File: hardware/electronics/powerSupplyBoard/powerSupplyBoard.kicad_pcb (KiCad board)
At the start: 4 copper layers, 100 x 50 mm, 119 parts, among them J1 USB_C_Receptacle_USB2.0, J10 1729018, J11 PREC002SAAN-RC, J3 615004143821, J4 PRPC009SBAN-M71RC, J5 Barrel_Jack_Switch, J6 S2B-PH-SM4-TB, J7 PREC002SAAN-RC, J8 PREC003SAAN-RC, J9 S3B-XH-SM4-TB, Q1 BUK961R6, Q2 CSD18532Q5B, Q3 CSD18532Q5B, Q4 BSS84, Q5 2N7002, Q6 2N7002, SW1 PTS647, SW2 SS-12D07, U1 STM32L052K6, U2 AP2112K-3.3, U3 SN65HVD230QDR, U4 BQ25798, U5 BQ76905, U6 BQ34Z100-R2, Y1 ECS-327ATQMV

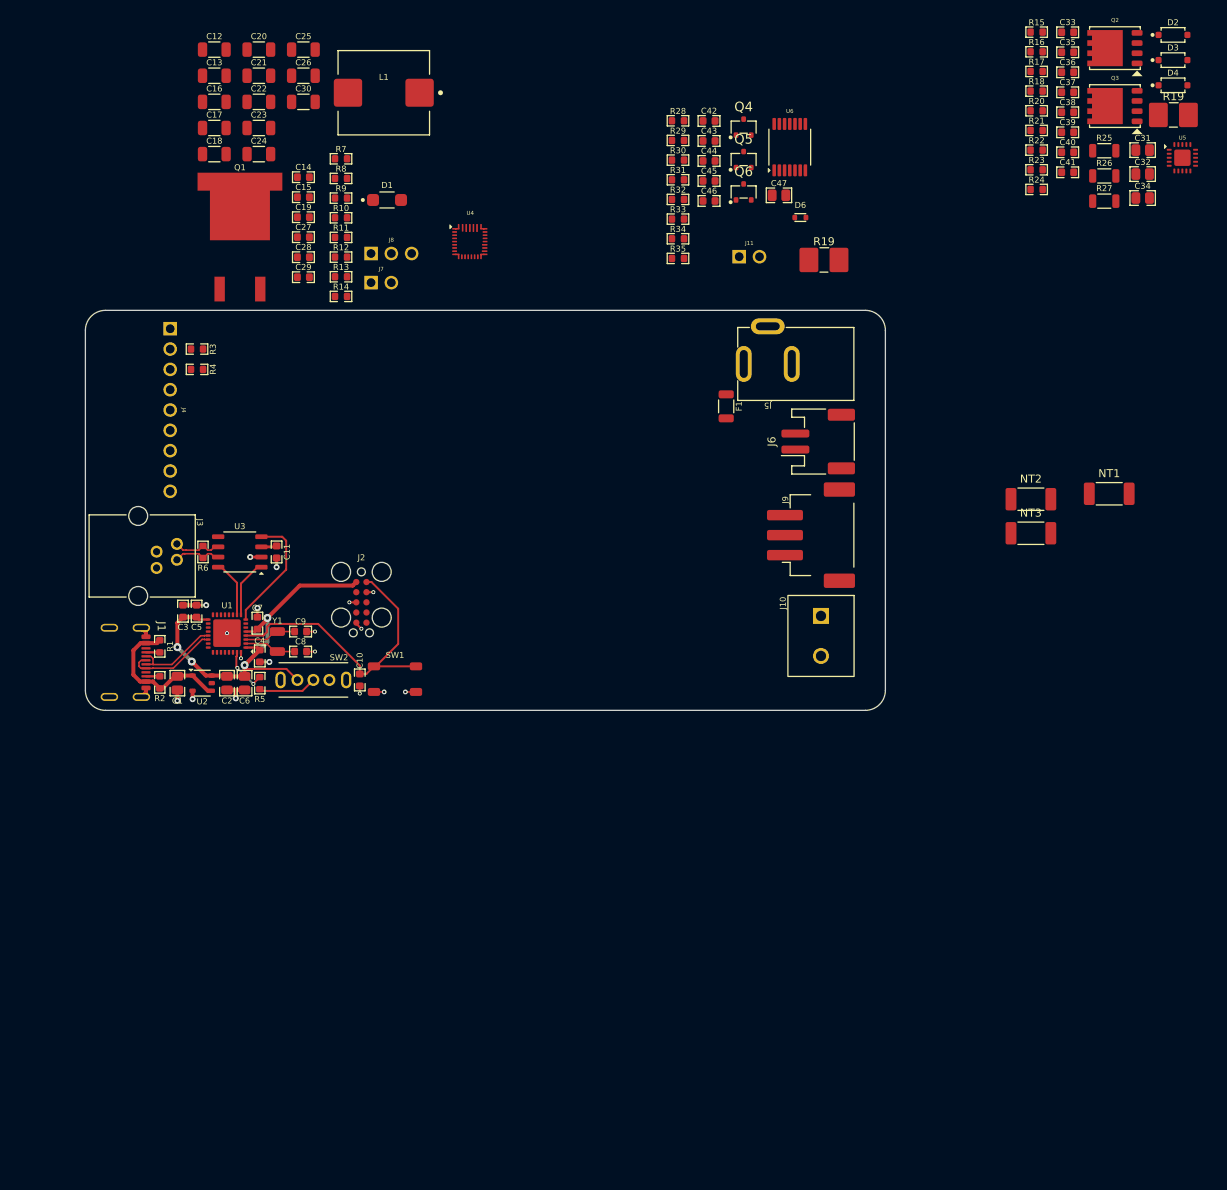
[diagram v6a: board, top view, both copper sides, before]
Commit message: re-synced board. adjusted reference labels
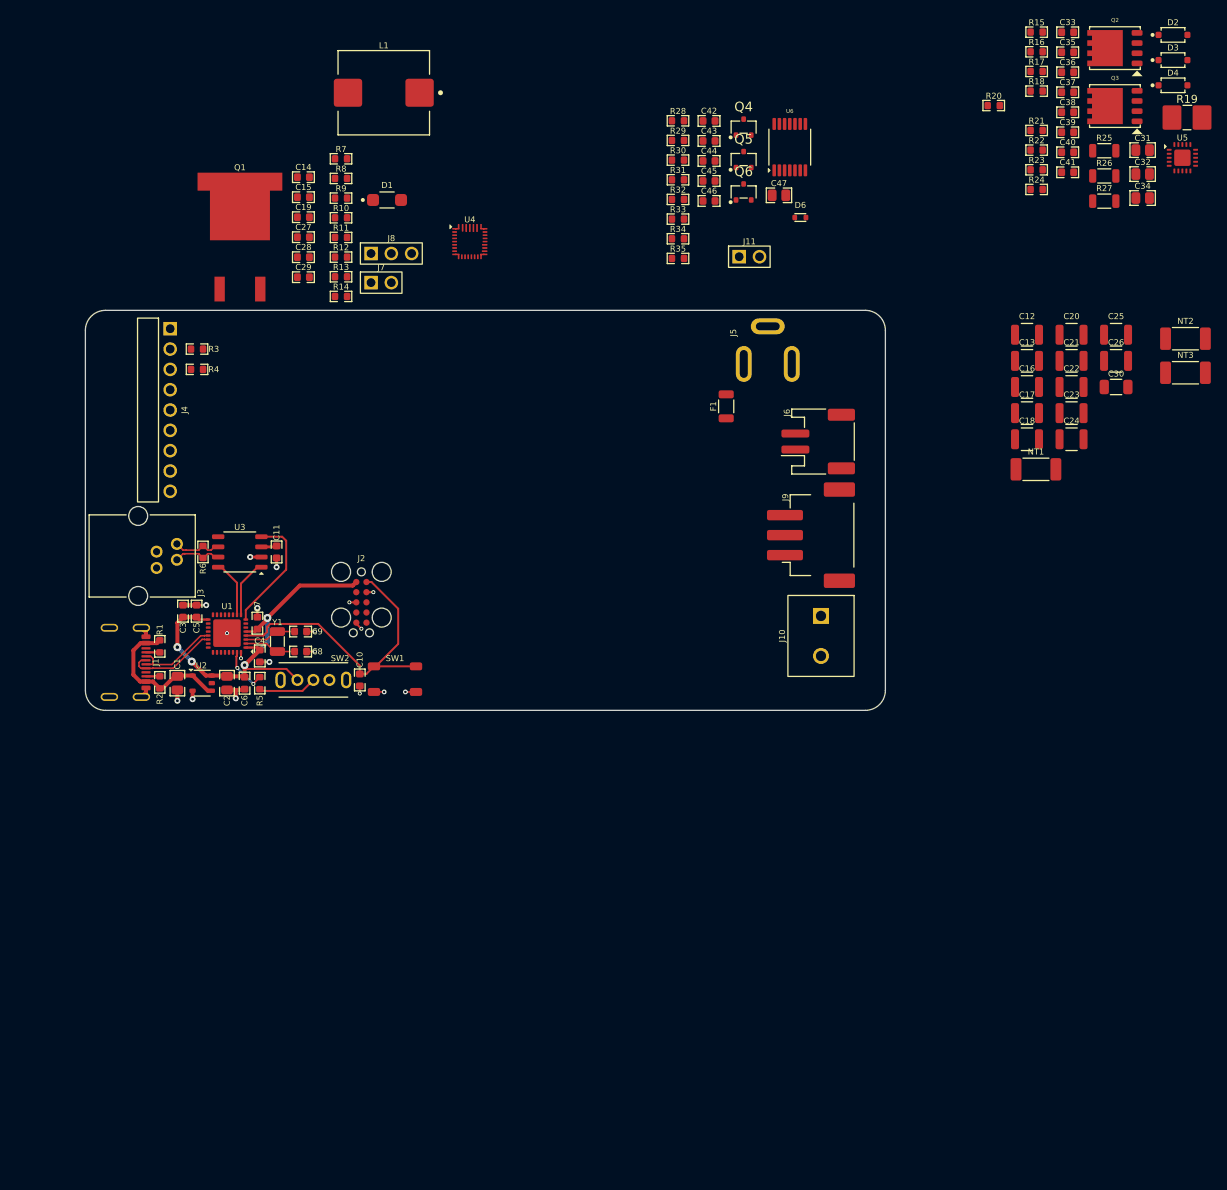
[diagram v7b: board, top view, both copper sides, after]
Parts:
- removed the R19 at (221.0, 25.6)
- C1, C2, C31, C32, C34, C47: footprint DS-Capacitors-SMD:MLCC0805 -> lib_fp:MLCC0805
- C10, C11, C14, C15, C19, C27, C28, C29, C3, C33, C35, C36, C37, C38, C39, C4, C40, C41, C42, C43, C44, C45, C46, C5, C7, C8, C9: footprint DS-Capacitors-SMD:MLCC0603 -> lib_fp:MLCC0603
- C12, C13, C16, C17, C18, C20, C21, C22, C23, C24, C25, C26: footprint DS-Capacitors-SMD:MLCC1206 -> lib_fp:MLCC1210
- C30: footprint DS-Capacitors-SMD:MLCC1206 -> lib_fp:MLCC1206
- C6: footprint DS-Capacitors-SMD:MLCC0805 -> lib_fp:MLCC0603
- D1: footprint DS-LED-SMD:LTST-1206 -> lib_fp:LTST-1206
- D2, D3, D4: footprint DS-Package-SO:SOD123 -> lib_fp:SOD123
- D6: footprint DS-Package-SO:SOD523 -> lib_fp:SOD523
- F1: footprint DS-Fuses:PTS1206 -> lib_fp:PTS1206
- J1: footprint DS-Connector-USB:MOLEX_2171790001 -> lib_fp:MOLEX_2171790001
- J10: footprint DS-Rectangular-Connectors:5mmTerminalBlock -> lib_fp:5mmTerminalBlock
- J11, J7: footprint DS-Rectangular-Connectors:conn_01x02_254 -> lib_fp:conn_01x02_254
- J2: footprint DS-Connectors-SMD:TC2050-FP -> lib_fp:TC2050-FP
- J3: footprint DS-Connectors-Network:615004143821 -> lib_fp:615004143821
- J4: footprint DS-Rectangular-Connectors:conn_01x09_254_right_angle -> lib_fp:conn_01x09_254_right_angle
- J5: footprint DS-Battery-Connectors:PJ-002A -> lib_fp:PJ-002A
- J6: footprint DS-Rectangular-Connectors:JST-PH-S2B-SM4-TB -> lib_fp:JST-PH-S2B-SM4-TB
- J8: footprint DS-Rectangular-Connectors:conn_01x03_254 -> lib_fp:conn_01x03_254
- J9: footprint DS-Rectangular-Connectors:JST_XH_S3B-SM4-TB -> lib_fp:JST_XH_S3B-SM4-TB
- L1: footprint DS-Inductors-SMD:HCM1A1105V2 -> lib_fp:HCM1A1105V2
- NT1, NT2, NT3: footprint DS-Resistors-SMD:CRCW1210 -> lib_fp:CRCW2010
- Q1: footprint DS-Package-SO:SOT404 -> lib_fp:SOT404
- Q2, Q3: footprint DS-Package-SO:SON8P127_500X600X100L56X41N -> lib_fp:SON8P127_500X600X100L56X41N
- Q4, Q5, Q6: footprint DS-Package-SO:SOT23-3P95_290X130L43X40N -> lib_fp:SOT23-3P95_290X130L43X40N
- R1, R10, R12, R13, R14, R15, R16, R17, R18, R2, R20, R21, R22, R23, R24, R28, R29, R3, R30, R31, R32, R33, R34, R35, R4, R5, R6, R7, R8, R9: footprint DS-Resistors-SMD:CRCW0603 -> lib_fp:CRCW0603
- R11: value 127K -> 187K; footprint DS-Resistors-SMD:CRCW0603 -> lib_fp:CRCW0603
- R19: footprint DS-Resistors-SMD:WSLHP2010 -> lib_fp:WSLHP2010
- R25, R26, R27: footprint DS-Resistors-SMD:CRCW1206 -> lib_fp:CRCW1206
- SW1: footprint DS-Switches:SW_4.5x4.5 -> lib_fp:SW_4.5x4.5
- SW2: footprint DS-Switches:SS-12D07-VG_GA_PA -> lib_fp:SS-12D07-VG_GA_PA
- U1: footprint DS-Microcontrollers:UFQFPN32 -> lib_fp:UFQFPN32
- U2: footprint DS-Package-SO:SOT23-5P95_280X300X110L40X38N -> lib_fp:SOT23-5P95_280X300X110L40X38N
- U3: footprint DS-Package-SO:SOIC8P127_490X600X195L83X42N -> lib_fp:SOIC8P127_490X600X195L83X42N
- U4: footprint DS-PMIC-SMD:RQM0029A -> lib_fp:RQM0029A
- U5: footprint DS-PMIC-SMD:RGR0020A -> lib_fp:RGR0020A
- U6: footprint DS-Package-SO:TSSOP14P65_500x640X120L150X45N -> lib_fp:TSSOP14P65_500x640X120L150X45N
- Y1: footprint DS-Crystals:EXC-34Q -> lib_fp:EXC-34Q
- moved C12 107.7 mm to (202.7, 53.0)
- moved C13 107.7 mm to (202.7, 56.3)
- moved C16 107.7 mm to (202.7, 59.6)
- moved C17 107.7 mm to (202.7, 62.8)
- moved C18 107.7 mm to (202.7, 66.1)
- moved C20 107.7 mm to (208.3, 53.0)
- moved C21 107.7 mm to (208.3, 56.3)
- moved C22 107.7 mm to (208.3, 59.6)
- moved C23 107.7 mm to (208.3, 62.8)
- moved C24 107.7 mm to (208.3, 66.1)
- moved C25 107.7 mm to (213.8, 53.0)
- moved C26 107.7 mm to (213.8, 56.3)
- moved C30 107.7 mm to (213.8, 59.6)
- moved R19 48.7 mm to (222.7, 25.9)
- moved NT2 27.9 mm to (222.5, 53.5)
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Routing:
- net VSS: vias 11 -> 18
- net GND: vias 7 -> 0

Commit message: layout for batt charger and connector labels
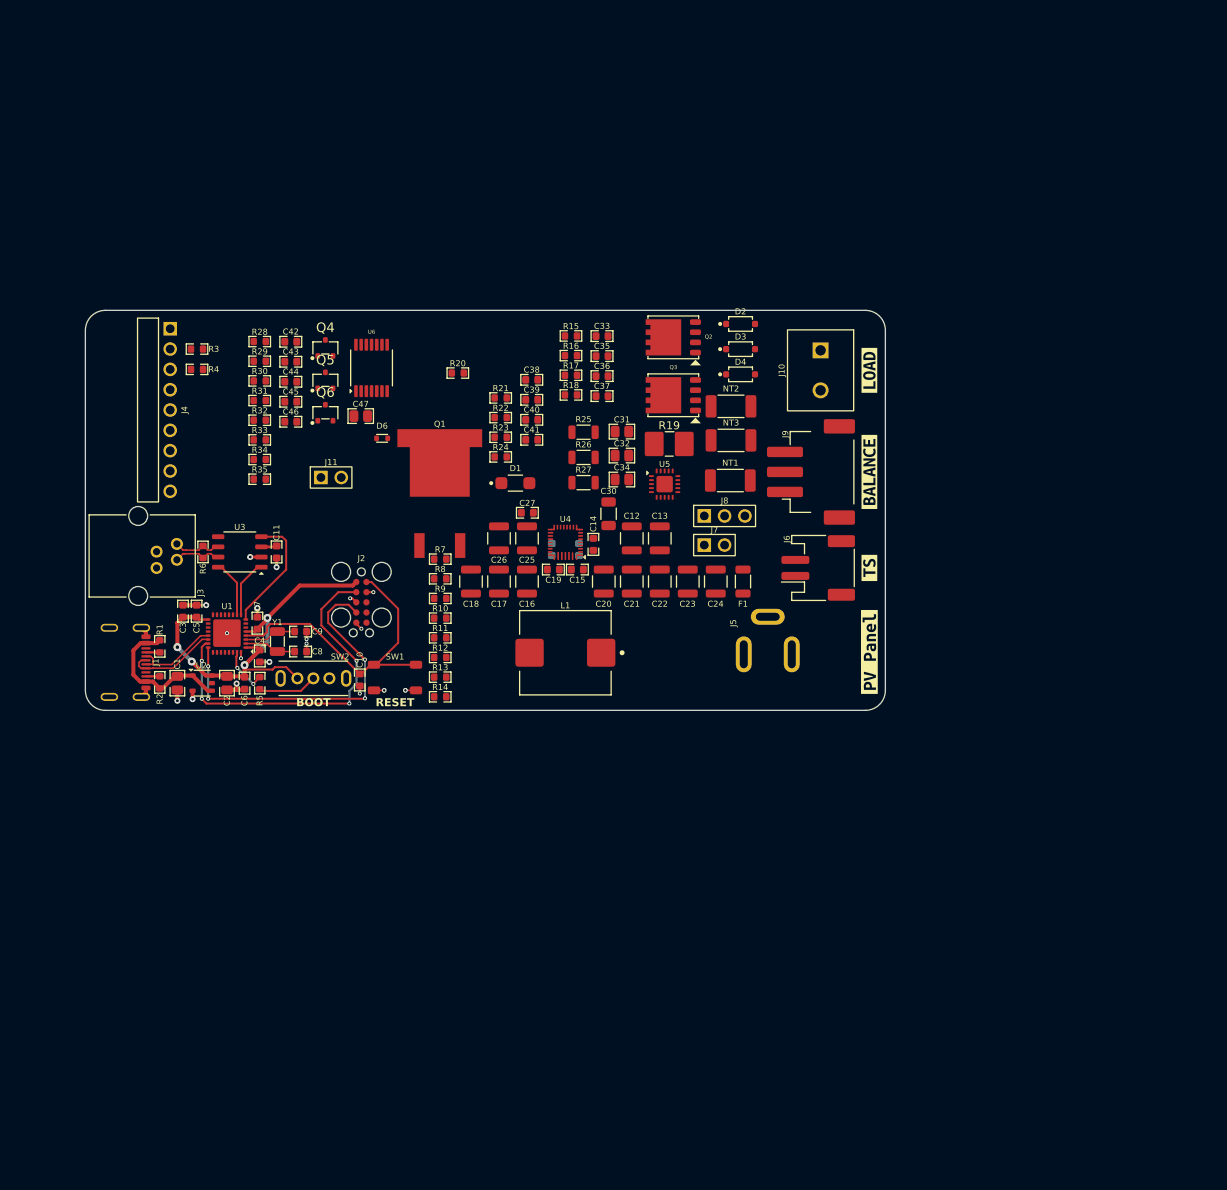
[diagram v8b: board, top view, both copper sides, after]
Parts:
- added kibuzzard-67280EE7: G***, kibuzzard-67280EE7, F.Cu at (183.0, 92.7)
- added kibuzzard-67280F10: G***, kibuzzard-67280F10, F.Cu at (183.0, 57.5)
- added kibuzzard-67280F1F: G***, kibuzzard-67280F1F, F.Cu at (183.0, 70.2)
- added kibuzzard-67280F3F: G***, kibuzzard-67280F3F, F.Cu at (183.0, 82.2)
- C28, C29: moved to B.Cu
- moved C26 80.3 mm to (136.7, 78.5), turned to 90 degrees
- moved C25 77.9 mm to (140.2, 78.5), turned to 90 degrees
- moved R19 76.5 mm to (158.0, 66.7)
- moved U5 76.5 mm to (157.4, 71.7)
- moved R21 74.9 mm to (136.9, 60.9)
- moved R22 74.9 mm to (136.9, 63.4)
- moved R23 74.9 mm to (136.9, 65.9)
- moved R24 74.9 mm to (136.9, 68.3)
- moved C38 74.9 mm to (140.8, 58.7)
- moved C39 74.9 mm to (140.8, 61.2)
- moved C40 74.9 mm to (140.8, 63.7)
- moved C41 74.9 mm to (140.8, 66.2)
- moved R20 74.9 mm to (131.6, 57.8)
- moved C31 74.0 mm to (152.1, 65.2)
- moved C32 74.0 mm to (152.1, 68.2)
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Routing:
- net /SWDIO: track 0.00 -> 45.3 mm, vias 0 -> 4
- net /SWDCLK: track 0.00 -> 43.0 mm, vias 0 -> 4
- net /NRST: track 39.8 -> 39.1 mm
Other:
- board text added: "BOOT"
- board text added: "RESET"
